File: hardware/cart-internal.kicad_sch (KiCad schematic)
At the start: 9 parts, among them J4 debug-snoop, P1 edge connector, U1 74LVC138A, U2 MCP1827S-3302E/EB

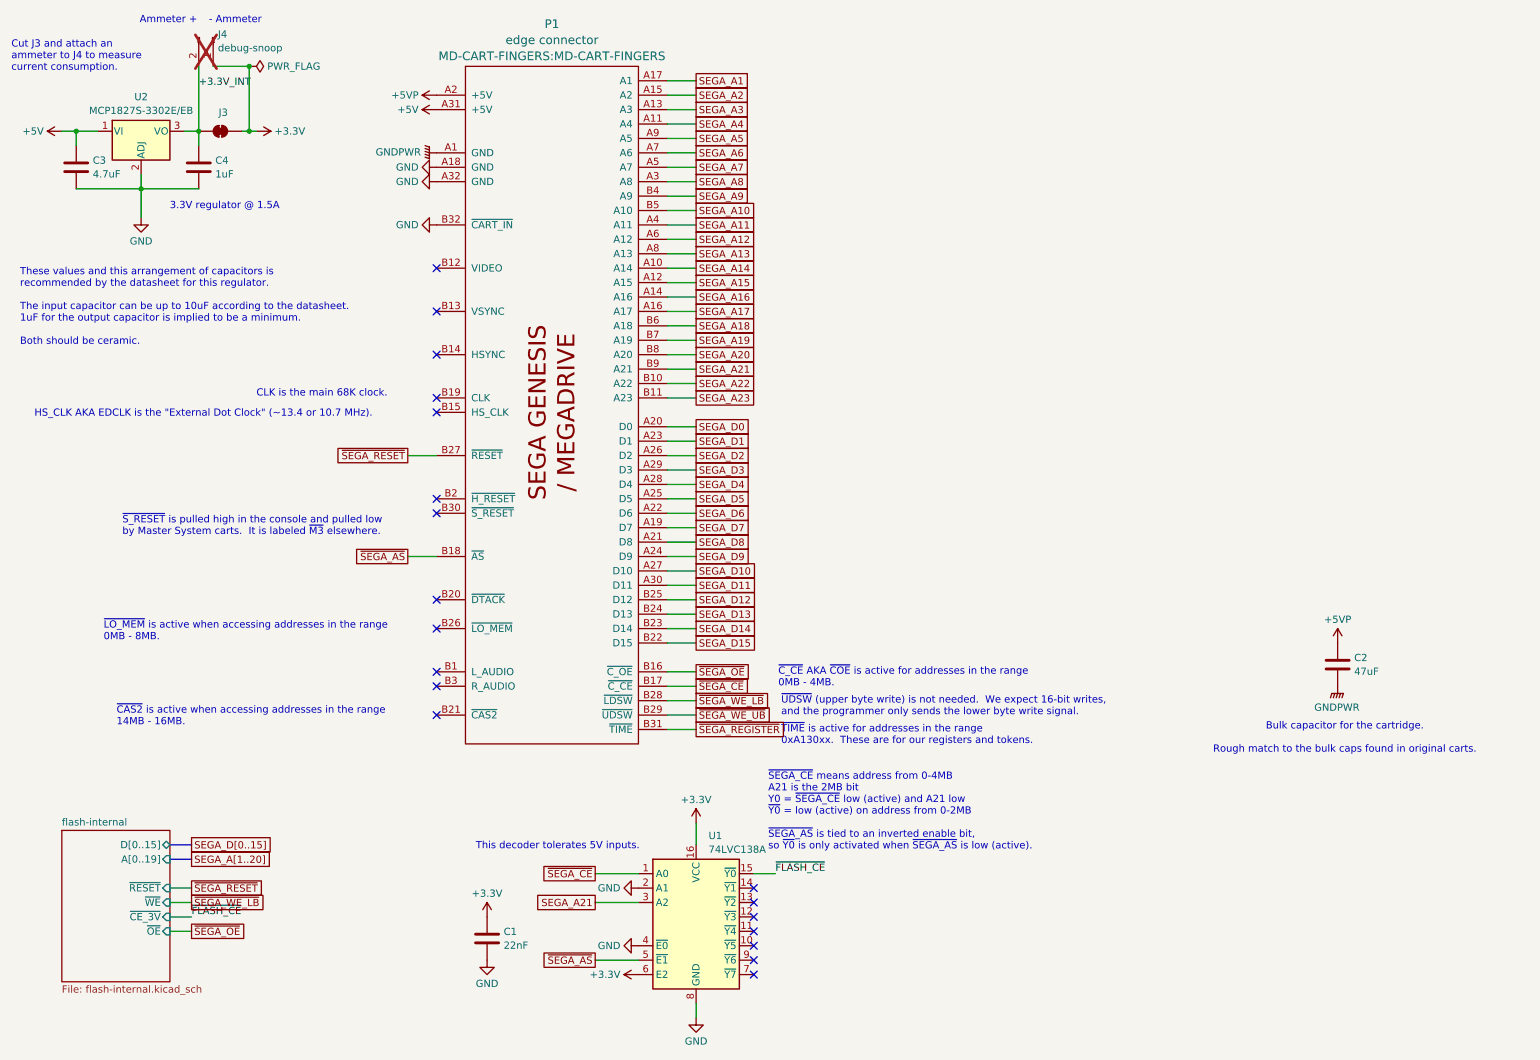
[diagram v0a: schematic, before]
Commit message: Reannotate schematics and drop debug bridges
Parts are now numbered starting at 0 for cart, 100 for SRAM, 300 for
microcontroller.

Also, drop debug bridges that made routing more difficult and had the
same names across prototype boards.

Hopefully this will help avoid naming conflicts for the unified PCB.

Also, redo prototype PCB layouts.

Now that all the names have changed, update board layouts.
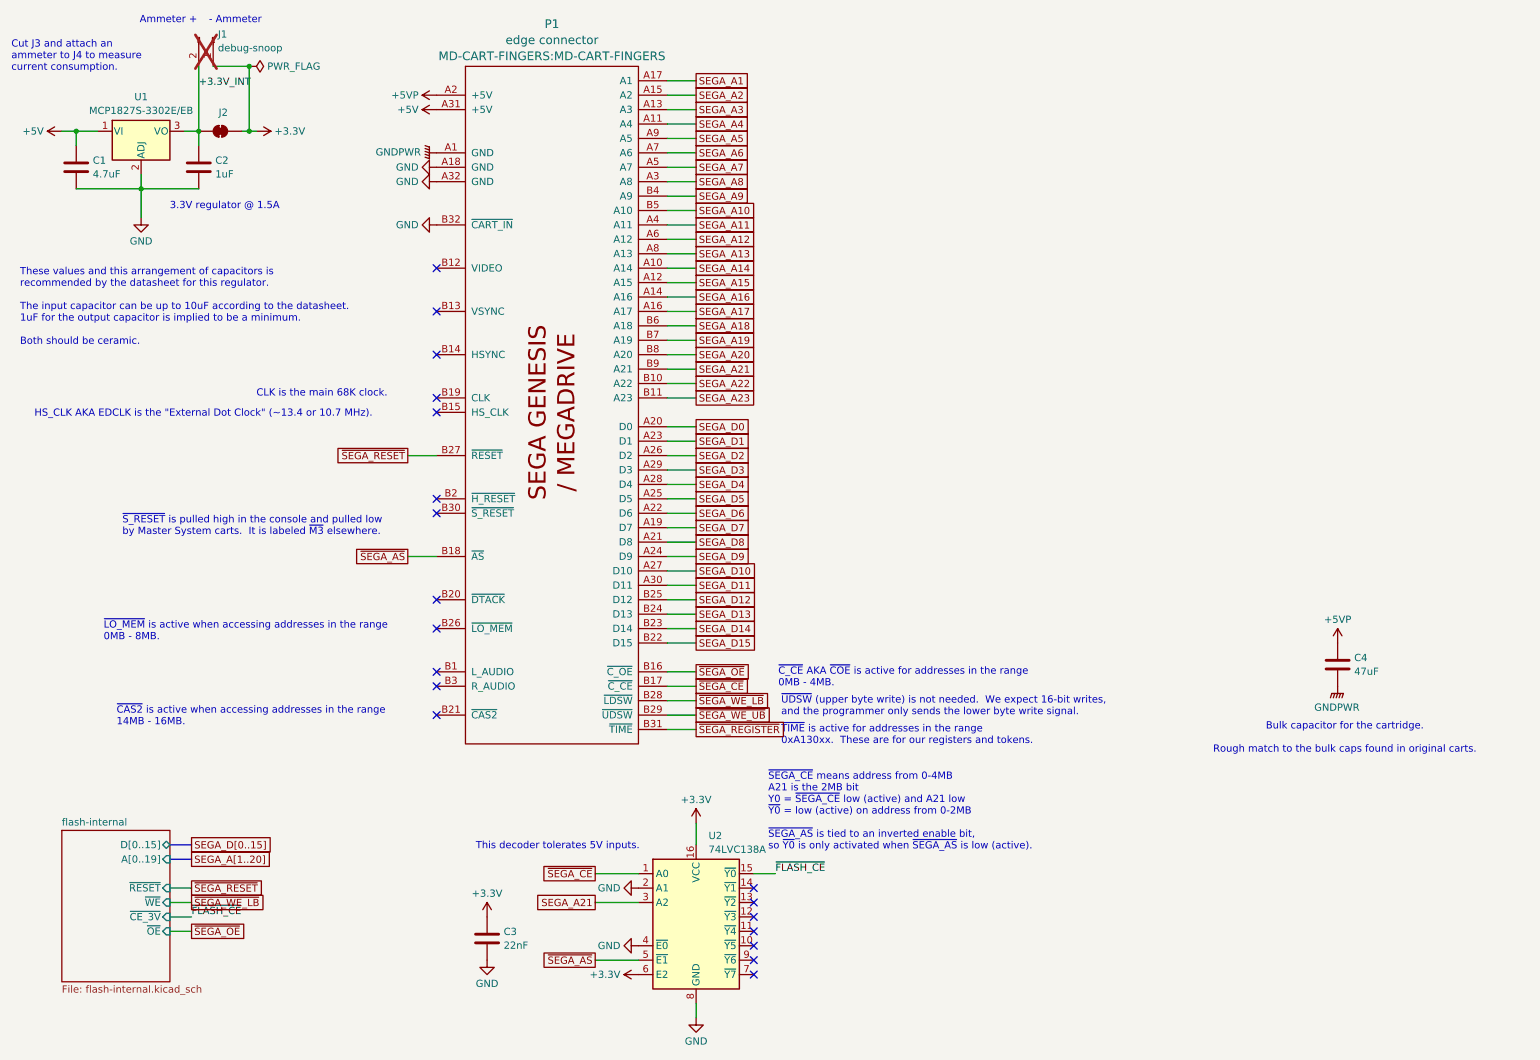
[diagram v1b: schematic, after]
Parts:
- renumbered C3 to C1, C4 to C2, C1 to C3, C2 to C4, J4 to J1, J3 to J2, U2 to U1, U1 to U2

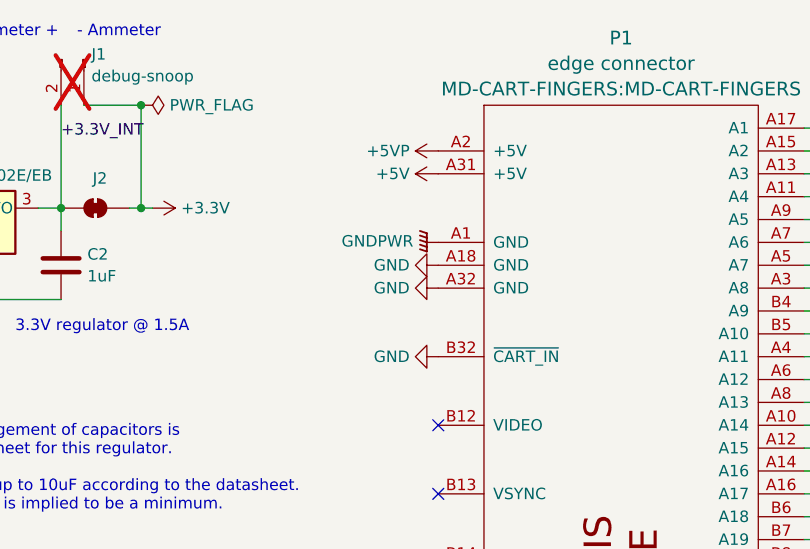
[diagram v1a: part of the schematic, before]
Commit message: Drop A18 GND connection
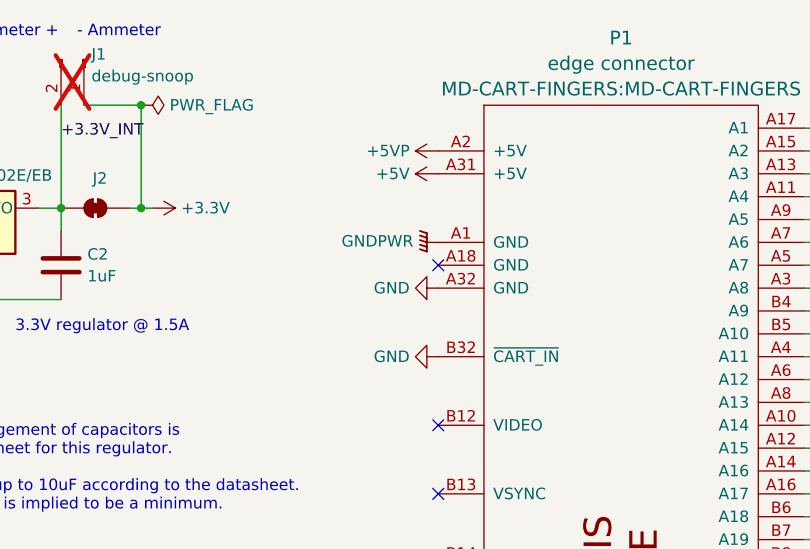
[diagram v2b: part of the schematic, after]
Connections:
- net GND: no longer P1.A18 (GND)
- no-connect marks 19 -> 20
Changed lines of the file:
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@@
+	)
+	(no_connect
+		(at 90.17 40.64)
 	)
 	(no_connect
@@
 					(unit 1)
 				)
-			)
-		)
-	)
-	(symbol
-		(lib_id "power:GND")
-		(at 90.17 40.64 270)
-		(unit 1)
-		(exclude_from_sim no)
-		(in_bom yes)
-		(on_board yes)
-		(dnp no)
-		(fields_autoplaced yes)
-		(property "Reference" "#PWR013"
-			(at 83.82 40.64 0)
-			(effects
-				(font
-					(size 1.27 1.27)
-				)
-				(hide yes)
-			)
-		)
-		(property "Value" "GND"
-			(at 86.9951 40.64 90)
-			(effects
-				(font
-					(size 1.27 1.27)
-				)
-				(justify right)
-			)
-		)
-		(property "Footprint" ""
-			(at 90.17 40.64 0)
-			(effects
-				(font
-					(size 1.27 1.27)
-				)
-				(hide yes)
-			)
-		)
-		(property "Datasheet" ""
-			(at 90.17 40.64 0)
-			(effects
-				(font
-					(size 1.27 1.27)
-				)
-				(hide yes)
-			)
-		)
-		(property "Description" "Power symbol creates a global label with name \"GND\" , ground"
-			(at 90.17 40.64 0)
-			(effects
-				(font
-					(size 1.27 1.27)
-				)
-				(hide yes)
-			)
-		)
-		(pin "1"
-		)
-		(instances
-			(project "cart"
-				(path "/686046a3-64dc-4761-a4ce-3e2fd65204d5/e9fa6217-2f64-413a-b493-80c4dcbbade7"
-					(reference "#PWR013")
-					(unit 1)
-				)
-			)
-			(project "cart"
-				(path "/6dac8cb5-ba7e-4a0d-b8d8-ab0b7982aa02/3dd377c9-146d-4660-b577-1c8ceb8667c0"
-					(reference "#PWR013")
-					(unit 1)
-				)
